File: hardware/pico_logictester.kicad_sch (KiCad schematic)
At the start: 0 parts

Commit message: hardware: Eingänge beschaltet, und tft angeschlossen
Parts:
- added A?: RaspberryPi_Pico, Module:RaspberryPi_Pico_Common_Unspecified, symbol MCU_Module:RaspberryPi_Pico
- added J?: TFT Display, symbol Connector_Generic:Conn_01x08
- added J? (x2): Conn_01x08, symbol Connector_Generic:Conn_01x08
- added R? (x8): 1k, symbol Device:R
- added R?: 33, symbol Device:R
- added RN?: R_Pack08, symbol Device:R_Pack08
- added RN? (x2): R_Network08, Resistor_THT:R_Array_SIP9, symbol Device:R_Network08
- added U? (x2): 74HC245, symbol 74xx:74HC245
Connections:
- new net: J?.1 (Pin_1), R?.2 (x2)
- new net: J?.2 (Pin_2), R?.2
- new net: J?.3 (Pin_3), R?.2
- new net: J?.4 (Pin_4), R?.2
- new net: J?.5 (Pin_5), R?.2
- new net: J?.6 (Pin_6), R?.2
- new net: J?.7 (Pin_7), R?.2
- new net: J?.8 (Pin_8), R?.2
- new net: R?.1, RN?.6 (R5), U?.15 (B3)
- new net: J?.8 (Pin_8), RN?.1 (R1.1)
- new net: RN?.10 (R7.2), RN?.8 (R7), U?.17 (B1)
- new net: RN?.11 (R6.2), RN?.7 (R6), U?.16 (B2)
- new net: RN?.12 (R5.2), RN?.6 (R5), U?.15 (B3)
- new net: RN?.13 (R4.2), RN?.5 (R4), U?.14 (B4)
- new net: RN?.14 (R3.2), RN?.4 (R3), U?.13 (B5)
- new net: RN?.15 (R2.2), RN?.3 (R2), U?.12 (B6)
- new net: RN?.16 (R1.2), RN?.2 (R1), U?.11 (B7)
- new net: J?.7 (Pin_7), RN?.2 (R2.1)
- new net: J?.6 (Pin_6), RN?.3 (R3.1)
- new net: J?.5 (Pin_5), RN?.4 (R4.1)
- new net: J?.4 (Pin_4), RN?.5 (R5.1)
- new net: J?.3 (Pin_3), RN?.6 (R6.1)
- new net: J?.2 (Pin_2), RN?.7 (R7.1)
- new net: J?.1 (Pin_1), RN?.8 (R8.1)
- new net: RN?.9 (R8), RN?.9 (R8.2), U?.18 (B0)
- new net: R?.1, RN?.3 (R2), U?.12 (B6)
- new net: R?.1, RN?.9 (R8), U?.18 (B0)
- new net: R?.1, RN?.2 (R1), U?.11 (B7)
- new net: R?.1, RN?.4 (R3), U?.13 (B5)
- new net: R?.1, RN?.5 (R4), U?.14 (B4)
- new net: R?.1, RN?.7 (R6), U?.16 (B2)
- new net: R?.1, RN?.8 (R7), U?.17 (B1)
- new net +3.3V: A?.36 (3V3), J?.7 (Pin_7), R?.1, U?.20 (VCC), U?.20 (VCC)
- new net +5V: A?.39 (VSYS)
- new net GND: A?.13 (GND), A?.18 (GND), A?.23 (GND), A?.28 (GND), A?.3 (GND), A?.33 (AGND), A?.38 (GND), A?.8 (GND), J?.8 (Pin_8), RN?.1 (common), RN?.1 (common), U?.1 (A->B), U?.1 (A->B), U?.10 (GND), U?.10 (GND), U?.19 (CE), U?.19 (CE)
- new net TFT_CS: A?.4 (GPIO2), J?.2 (Pin_2)
- new net TFT_DC: A?.5 (GPIO3), J?.3 (Pin_3)
- new net TFT_RST: A?.6 (GPIO4), J?.4 (Pin_4)
- new net TFT_SDCLK: A?.24 (GPIO18), J?.6 (Pin_6)
- new net TFT_SDIN: A?.25 (GPIO19), J?.5 (Pin_5)
- no-connect marks 0 -> 3

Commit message: hardware: Alle baugruppen im schaltplan hinzugefügt.
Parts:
- added C? (x2): 100n, symbol Device:C
- added C? (x2): 10u, symbol Device:C_Polarized
- added D? (x2): 1N4148, Diode_THT:D_DO-35_SOD27_P7.62mm_Horizontal, symbol Diode:1N4148
- added D?: 3,3, symbol Device:D_Zener
- added J? (x2): Conn_01x02, symbol Connector_Generic:Conn_01x02
- added Q?: AO3401A, Package_TO_SOT_SMD:SOT-23, symbol Transistor_FET:AO3401A
- added Q?: BC547, Package_TO_SOT_THT:TO-92_Inline, symbol Transistor_BJT:BC547
- added R? (x3): 10k, symbol Device:R
- added R? (x2): 1k, symbol Device:R
- added SW?: SW_Push, symbol Switch:SW_Push
- RN?: value R_Pack08 -> 1k
- RN?: value R_Network08 -> 10k
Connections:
- net +3.3V: now also C?.1, C?.1, C?.1, C?.1
- net GND: now also C?.2, C?.2, C?.2, C?.2, D?.2 (A), J?.2 (Pin_2), J?.2 (Pin_2), Q?.3 (E), R?.2, SW?.1
- net SYSTEM_POWER_PIN: now reaches A?.1 (GPIO0)
- net SYSTEM_POWER_PIN: now also R?.1
- net LOGIC_1: now reaches A?.10 (GPIO7)
- net LOGIC_1: now also U?.3 (A1)
- net LOGIC_2: now reaches A?.11 (GPIO8)
- net LOGIC_2: now also U?.4 (A2)
- net LOGIC_3: now reaches A?.12 (GPIO9)
- net LOGIC_3: now also U?.5 (A3)
- net LOGIC_4: now reaches A?.14 (GPIO10)
- net LOGIC_4: now also U?.6 (A4)
- net LOGIC_5: now reaches A?.15 (GPIO11)
- net LOGIC_5: now also U?.7 (A5)
- net LOGIC_6: now reaches A?.16 (GPIO12)
- net LOGIC_6: now also U?.8 (A6)
- net LOGIC_7: now reaches A?.17 (GPIO13)
- net LOGIC_7: now also U?.9 (A7)
- net LOGIC_8: now reaches A?.19 (GPIO14)
- net LOGIC_8: now also U?.2 (A0)
- net SENSE_GPIO: now reaches A?.2 (GPIO1)
- net SENSE_GPIO: now also D?.1 (K), R?.1
- net LOGIC_9: now reaches A?.20 (GPIO15)
- net LOGIC_9: now also U?.3 (A1)
- net LOGIC_10: now reaches A?.21 (GPIO16)
- net LOGIC_10: now also U?.4 (A2)
- net LOGIC_11: now reaches A?.22 (GPIO17)
- net LOGIC_11: now also U?.5 (A3)
- net LOGIC_12: now reaches A?.26 (GPIO20)
- net LOGIC_12: now also U?.6 (A4)
- net LOGIC_13: now reaches A?.27 (GPIO21)
- net LOGIC_13: now also U?.7 (A5)
- net LOGIC_14: now reaches A?.29 (GPIO22)
- net LOGIC_14: now also U?.8 (A6)
- net LOGIC_15: now reaches A?.31 (GPIO26_ADC0)
- net LOGIC_15: now also U?.9 (A7)
- net BAT_VOLTAGE: now reaches A?.32 (GPIO27_ADC1)
- net BAT_VOLTAGE: now also R?.1, R?.2
- net LOGIC_0: now reaches A?.9 (GPIO6)
- net LOGIC_0: now also U?.2 (A0)
- new net: D?.1 (K), Q?.1 (C)
- new net: D?.2 (A), D?.2 (A), Q?.1 (G), R?.1
- new net: D?.1 (K), R?.2, SW?.2
- new net: Q?.2 (B), R?.2
- new net AKKU+: J?.1 (Pin_1), Q?.2 (S), R?.1, R?.2
- new net STEP_UP_5V: J?.1 (Pin_1), Q?.3 (D)
- no-connect marks 3 -> 6
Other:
- moved on the sheet: A?, J?, R?, RN?, U?

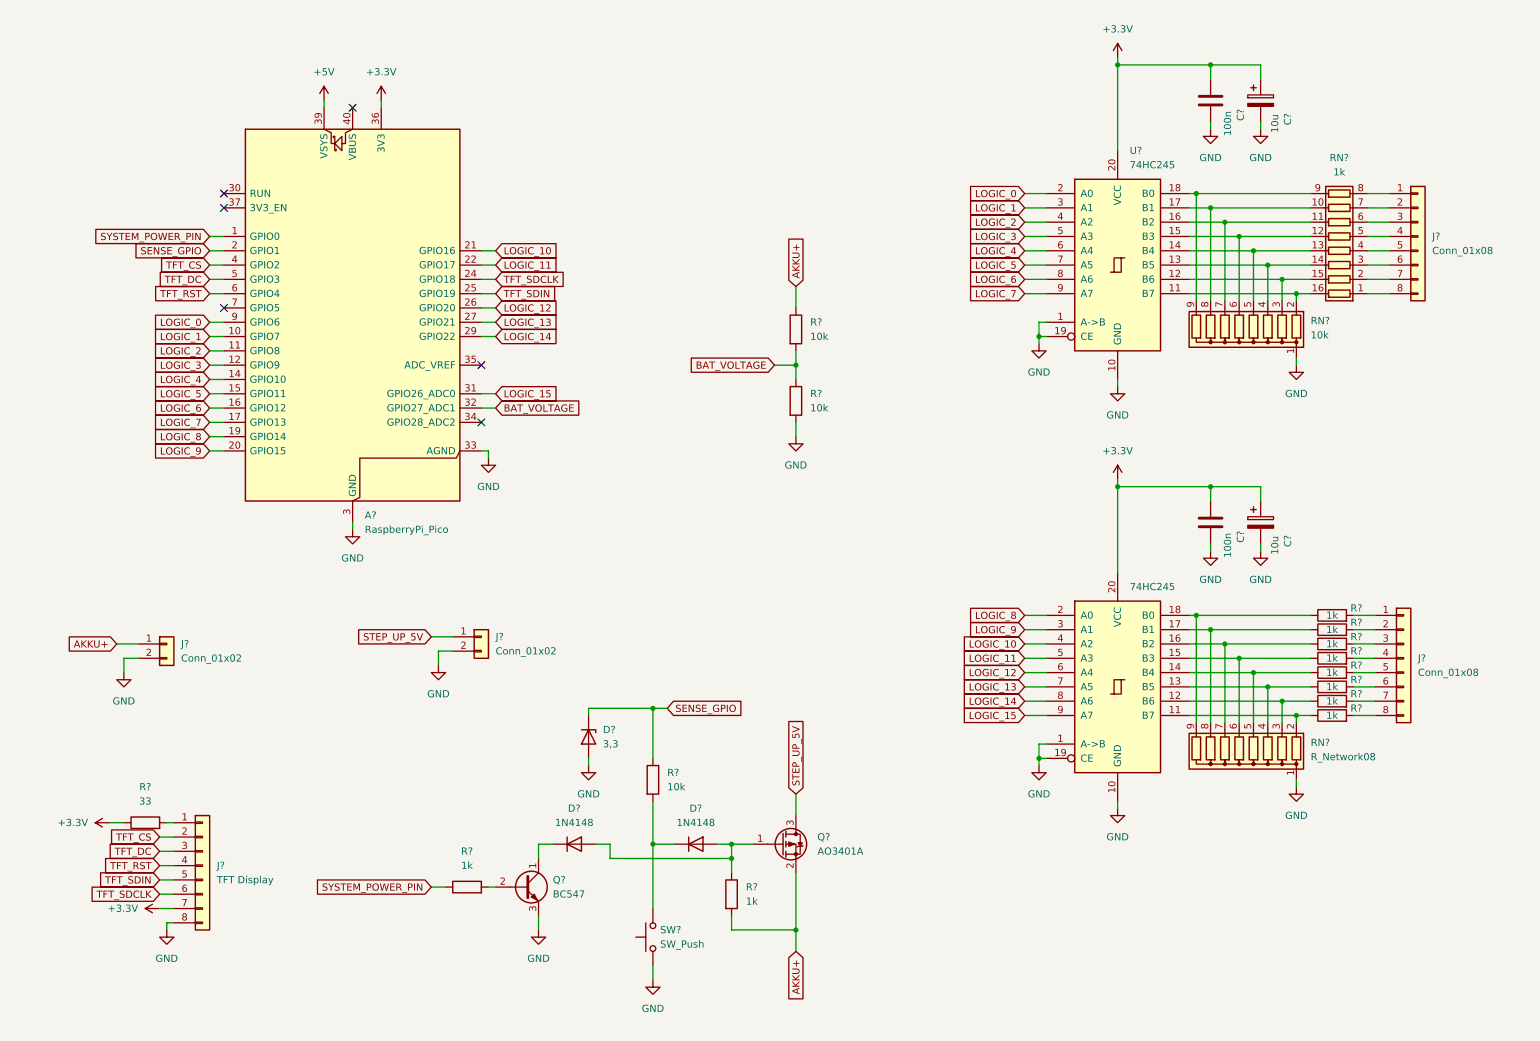
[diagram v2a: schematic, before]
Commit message: hardware: Schaltplan fertig gestellt und Footprints zugeordnet
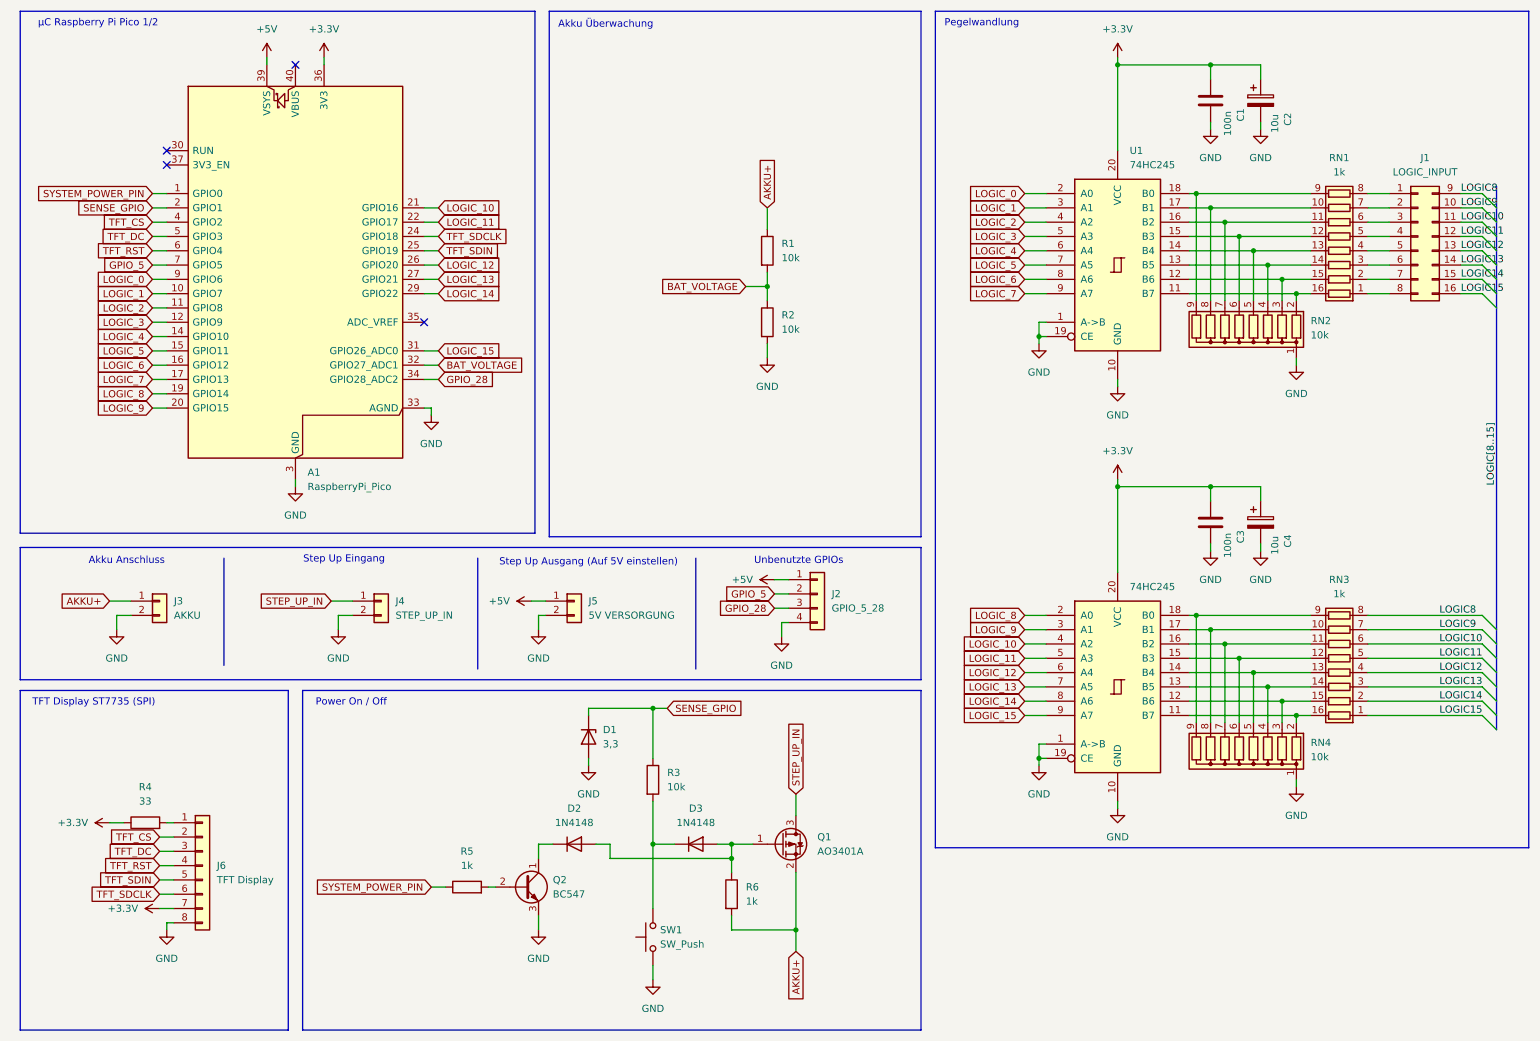
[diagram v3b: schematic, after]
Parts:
- removed J? (x2): Conn_01x08, symbol Connector_Generic:Conn_01x08
- removed R? (x8): 1k, symbol Device:R
- added J1: LOGIC_INPUT, connector_tk:PinHeader_2x08_P2.54mm_Horizontal_cw, symbol Connector_Generic:Conn_02x08_Top_Bottom
- added J2: GPIO_5_28, Connector_PinHeader_2.54mm:PinHeader_1x04_P2.54mm_Vertical, symbol Connector_Generic:Conn_01x04
- added J5: 5V VERSORGUNG, Connector_PinHeader_2.54mm:PinHeader_1x02_P2.54mm_Vertical, symbol Connector_Generic:Conn_01x02
- added RN3: 1k, Resistor_SMD:R_Array_Convex_8x0602, symbol Device:R_Pack08
- C1, C3: renamed from C?; footprint (none) -> Capacitor_SMD:C_0805_2012Metric_Pad1.18x1.45mm_HandSolder
- C2, C4: renamed from C?; footprint (none) -> Capacitor_SMD:CP_Elec_4x5.4
- D1: renamed from D?; footprint (none) -> Diode_THT:D_DO-35_SOD27_P7.62mm_Horizontal
- J3: renamed from J?; value Conn_01x02 -> AKKU; footprint (none) -> Connector_PinHeader_2.54mm:PinHeader_1x02_P2.54mm_Vertical
- J4: renamed from J?; value Conn_01x02 -> STEP_UP_IN; footprint (none) -> Connector_PinHeader_2.54mm:PinHeader_1x02_P2.54mm_Vertical
- J6: renamed from J?; footprint (none) -> Connector_PinSocket_2.54mm:PinSocket_1x08_P2.54mm_Vertical
- R1, R2, R3, R4, R5, R6: renamed from R?; footprint (none) -> Resistor_SMD:R_0805_2012Metric_Pad1.20x1.40mm_HandSolder
- RN1: renamed from RN?; footprint (none) -> Resistor_SMD:R_Array_Convex_8x0602
- RN4: renamed from RN?; value R_Network08 -> 10k
- SW1: renamed from SW?; footprint (none) -> Button_Switch_THT:SW_PUSH_6mm_H5mm
- U1, U2: renamed from U?; footprint (none) -> Package_SO:TSSOP-20_4.4x6.5mm_P0.65mm
- gave numbers to parts that had none: 6
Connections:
- net +5V: now also J2.1 (Pin_1), J5.1 (Pin_1)
- net GND: now also J2.4 (Pin_4), J5.2 (Pin_2)
- net at RN4.6 (R5), U2.15 (B3): now also RN3.12 (R5.2)
- net at RN1.1 (R1.1): now also J1.8 (Pin_8)
- net at RN1.2 (R2.1): now also J1.7 (Pin_7)
- net at RN1.3 (R3.1): now also J1.6 (Pin_6)
- net at RN1.4 (R4.1): now also J1.5 (Pin_5)
- net at RN1.5 (R5.1): now also J1.4 (Pin_4)
- net at RN1.6 (R6.1): now also J1.3 (Pin_3)
- net at RN1.7 (R7.1): now also J1.2 (Pin_2)
- net at RN1.8 (R8.1): now also J1.1 (Pin_1)
- net GPIO_28: now reaches A1.34 (GPIO28_ADC2)
- net GPIO_28: now also J2.3 (Pin_3)
- net GPIO_5: now reaches A1.7 (GPIO5)
- net GPIO_5: now also J2.2 (Pin_2)
- net at RN4.3 (R2), U2.12 (B6): now also RN3.15 (R2.2)
- net at RN4.9 (R8), U2.18 (B0): now also RN3.9 (R8.2)
- net at RN4.2 (R1), U2.11 (B7): now also RN3.16 (R1.2)
- net at RN4.4 (R3), U2.13 (B5): now also RN3.14 (R3.2)
- net at RN4.5 (R4), U2.14 (B4): now also RN3.13 (R4.2)
- net at RN4.7 (R6), U2.16 (B2): now also RN3.11 (R6.2)
- net at RN4.8 (R7), U2.17 (B1): now also RN3.10 (R7.2)
- net STEP_UP_5V renamed STEP_UP_IN
- new net LOGIC10: J1.11 (Pin_11), RN3.6 (R6.1)
- new net LOGIC11: J1.12 (Pin_12), RN3.5 (R5.1)
- new net LOGIC12: J1.13 (Pin_13), RN3.4 (R4.1)
- new net LOGIC13: J1.14 (Pin_14), RN3.3 (R3.1)
- new net LOGIC14: J1.15 (Pin_15), RN3.2 (R2.1)
- new net LOGIC15: J1.16 (Pin_16), RN3.1 (R1.1)
- new net LOGIC8: J1.9 (Pin_9), RN3.8 (R8.1)
- new net LOGIC9: J1.10 (Pin_10), RN3.7 (R7.1)
- no-connect marks 6 -> 4
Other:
- note added: "Akku Anschluss"
- note added: "Akku Überwachung"
- note added: "Pegelwandlung"
- note added: "Power On / Off"
- note added: "Step Up Ausgang (Auf 5V einstellen)"
- note added: "Step Up Eingang"
- note added: "TFT Display ST7735 (SPI)"
- note added: "Unbenutzte GPIOs"
- note added: "µC Raspberry Pi Pico 1/2"
- company: (none) -> Thorsten Kattanek
- title: (none) -> Pico Logictester
- moved on the sheet: A1, J3, J4, R1, R2

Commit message: Autorouting im Livestream. noch 6 offene Verbindungen!
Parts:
- removed J1: LOGIC_INPUT, connector_tk:PinHeader_2x08_P2.54mm_Horizontal_cw, symbol Connector_Generic:Conn_02x08_Top_Bottom
- added J1: LOGIC_INPUT, Connector_IDC:IDC-Header_2x08_P2.54mm_Horizontal, symbol Connector_Generic:Conn_02x08_Odd_Even
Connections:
- net LOGIC10: now also J1.6 (Pin_6)
- net LOGIC11: now also J1.8 (Pin_8)
- net LOGIC12: now also J1.10 (Pin_10)
- net LOGIC13: now also J1.12 (Pin_12)
- net LOGIC14: now also J1.14 (Pin_14)
- net LOGIC15: now also J1.16 (Pin_16)
- net LOGIC8: now also J1.2 (Pin_2)
- net LOGIC9: now also J1.4 (Pin_4)
- net at RN1.8 (R8.1): now also J1.1 (Pin_1)
- net at RN1.7 (R7.1): now also J1.3 (Pin_3)
- net at RN1.6 (R6.1): now also J1.5 (Pin_5)
- net at RN1.5 (R5.1): now also J1.7 (Pin_7)
- net at RN1.4 (R4.1): now also J1.9 (Pin_9)
- net at RN1.3 (R3.1): now also J1.11 (Pin_11)
- net at RN1.2 (R2.1): now also J1.13 (Pin_13)
- net at RN1.1 (R1.1): now also J1.15 (Pin_15)
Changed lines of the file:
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@@
 	)
 	(junction
+		(at 58.42 22.86)
+		(diameter 0)
+		(color 0 0 0 0)
+	)
+	(junction
 		(at 226.06 99.06)
 		(diameter 0)
@@
 	(wire
 		(pts
-			(xy 58.42 22.86) (xy 58.42 24.13)
+			(xy 58.42 21.59) (xy 58.42 22.86)
 		)
 		(stroke
@@
 	(wire
 		(pts
+			(xy 58.42 22.86) (xy 58.42 24.13)
+		)
+		(stroke
+			(width 0)
+			(type default)
+		)
+	)
+	(wire
+		(pts
 			(xy 86.36 52.07) (xy 88.9 52.07)
 		)
@@
 	(wire
 		(pts
+			(xy 54.61 22.86) (xy 58.42 22.86)
+		)
+		(stroke
+			(width 0)
+			(type default)
+		)
+	)
+	(wire
+		(pts
 			(xy 195.58 72.39) (xy 195.58 73.66)
 		)
@@
 	)
 	(symbol
-		(lib_id "Connector_Generic:Conn_02x08_Top_Bottom")
-		(at 262.89 54.61 0)
-		(unit 1)
-		(exclude_from_sim no)
-		(in_bom yes)
-		(on_board yes)
-		(dnp no)
-		(fields_autoplaced yes)
-		(property "Reference" "J1"
-			(at 264.16 40.64 0)
-			(effects
-				(font
-					(size 1.27 1.27)
-				)
-			)
-		)
-		(property "Value" "LOGIC_INPUT"
-			(at 264.16 43.18 0)
-			(effects
-				(font
-					(size 1.27 1.27)
-				)
-			)
-		)
-		(property "Footprint" "connector_tk:PinHeader_2x08_P2.54mm_Horizontal_cw"
-			(at 262.89 54.61 0)
-			(effects
-				(font
-					(size 1.27 1.27)
-				)
-				(hide yes)
-			)
-		)
-		(property "Datasheet" "~"
-			(at 262.89 54.61 0)
-			(effects
-				(font
-					(size 1.27 1.27)
-				)
-				(hide yes)
-			)
-		)
-		(property "Description" "Generic connector, double row, 02x08, top/bottom pin numbering scheme (row 1: 1...pins_per_row, row2: pins_per_row+1 ... num_pins), script generated (kicad-library-utils/schlib/autogen/connector/)"
-			(at 262.89 54.61 0)
-			(effects
-				(font
-					(size 1.27 1.27)
-				)
-				(hide yes)
-			)
-		)
-		(pin "6"
-		)
-		(pin "10"
-		)
-		(pin "16"
-		)
-		(pin "13"
-		)
-		(pin "3"
-		)
-		(pin "2"
-		)
-		(pin "11"
-		)
-		(pin "4"
-		)
-		(pin "7"
-		)
-		(pin "12"
-		)
-		(pin "9"
-		)
-		(pin "5"
-		)
-		(pin "8"
-		)
-		(pin "15"
-		)
-		(pin "1"
-		)
-		(pin "14"
-		)
-		(instances
-			(project ""
-				(path "/ab4c5817-8853-4523-896c-e7a16e8d82cb"
-					(reference "J1")
-					(unit 1)
-				)
-			)
-		)
-	)
-	(symbol
 		(lib_id "Connector_Generic:Conn_01x08")
 		(at 46.99 166.37 0)
@@
 	(symbol
 		(lib_id "power:+5V")
-		(at 58.42 22.86 0)
+		(at 58.42 21.59 0)
 		(unit 1)
 		(exclude_from_sim no)
@@
 		(fields_autoplaced yes)
 		(property "Reference" "#PWR03"
-			(at 58.42 26.67 0)
+			(at 58.42 25.4 0)
 			(effects
 				(font
@@
 		)
 		(property "Value" "+5V"
-			(at 58.42 17.78 0)
+			(at 58.42 16.51 0)
 			(effects
 				(font
@@
 		)
 		(property "Footprint" ""
-			(at 58.42 22.86 0)
+			(at 58.42 21.59 0)
 			(effects
 				(font
@@
 		)
 		(property "Datasheet" ""
-			(at 58.42 22.86 0)
+			(at 58.42 21.59 0)
 			(effects
 				(font
@@
 		)
 		(property "Description" "Power symbol creates a global label with name \"+5V\""
-			(at 58.42 22.86 0)
+			(at 58.42 21.59 0)
 			(effects
 				(font
@@
 	)
 	(symbol
+		(lib_id "power:PWR_FLAG")
+		(at 54.61 22.86 90)
+		(unit 1)
+		(exclude_from_sim no)
+		(in_bom yes)
+		(on_board yes)
+		(dnp no)
+		(fields_autoplaced yes)
+		(property "Reference" "#FLG01"
+			(at 52.705 22.86 0)
+			(effects
+				(font
+					(size 1.27 1.27)
+				)
+				(hide yes)
+			)
+		)
+		(property "Value" "PWR_FLAG"
+			(at 50.8 22.8599 90)
+			(effects
+				(font
+					(size 1.27 1.27)
+				)
+				(justify left)
+			)
+		)
+		(property "Footprint" ""
+			(at 54.61 22.86 0)
+			(effects
+				(font
+					(size 1.27 1.27)
+				)
+				(hide yes)
+			)
+		)
+		(property "Datasheet" "~"
+			(at 54.61 22.86 0)
+			(effects
+				(font
+					(size 1.27 1.27)
+				)
+				(hide yes)
+			)
+		)
+		(property "Description" "Special symbol for telling ERC where power comes from"
+			(at 54.61 22.86 0)
+			(effects
+				(font
+					(size 1.27 1.27)
+				)
+				(hide yes)
+			)
+		)
+		(pin "1"
+		)
+		(instances
+			(project ""
+				(path "/ab4c5817-8853-4523-896c-e7a16e8d82cb"
+					(reference "#FLG01")
+					(unit 1)
+				)
+			)
+		)
+	)
+	(symbol
 		(lib_id "power:GND")
 		(at 87.63 86.36 0)
@@
 					(unit 1)
 				)
+			)
+		)
+	)
+	(symbol
+		(lib_id "Connector_Generic:Conn_02x08_Odd_Even")
+		(at 262.89 54.61 0)
+		(unit 1)
+		(exclude_from_sim no)
+		(in_bom yes)
+		(on_board yes)
+		(dnp no)
+		(fields_autoplaced yes)
+		(property "Reference" "J1"
+			(at 264.16 40.64 0)
+			(effects
+				(font
+					(size 1.27 1.27)
+				)
+			)
+		)
+		(property "Value" "LOGIC_INPUT"
+			(at 264.16 43.18 0)
+			(effects
+				(font
+					(size 1.27 1.27)
+				)
+			)
+		)
+		(property "Footprint" "Connector_IDC:IDC-Header_2x08_P2.54mm_Horizontal"
+			(at 262.89 54.61 0)
+			(effects
+				(font
+					(size 1.27 1.27)
+				)
+				(hide yes)
+			)
+		)
+		(property "Datasheet" "~"
+			(at 262.89 54.61 0)
+			(effects
+				(font
+					(size 1.27 1.27)
+				)
+				(hide yes)
+			)
+		)
+		(property "Description" "Generic connector, double row, 02x08, odd/even pin numbering scheme (row 1 odd numbers, row 2 even numbers), script generated (kicad-library-utils/schlib/autogen/connector/)"
+			(at 262.89 54.61 0)
+			(effects
+				(font
+					(size 1.27 1.27)
+				)
+				(hide yes)
+			)
+		)
+		(pin "4"
+		)
+		(pin "12"
+		)
+		(pin "6"
+		)
+		(pin "2"
+		)
+		(pin "11"
+		)
+		(pin "13"
+		)
+		(pin "7"
+		)
+		(pin "1"
+		)
+		(pin "9"
+		)
+		(pin "14"
+		)
+		(pin "8"
+		)
+		(pin "16"
+		)
+		(pin "10"
+		)
+		(pin "15"
+		)
+		(pin "5"
+		)
+		(pin "3"
+		)
+		(instances
+			(project ""
+				(path "/ab4c5817-8853-4523-896c-e7a16e8d82cb"
+					(reference "J1")
+					(unit 1)
+				)
